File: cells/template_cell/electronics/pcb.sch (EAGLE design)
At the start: 28 parts, among them M1 M02PTH3, M2 M02PTH3, Q1 MOSFET-NCHANNEL2N7000, Q2 MOSFET-NCHANNEL2N7000, SW0 M01PTH_LONGPAD, SW1 M02PTH3, SW2 M02PTH3, SW3 M02PTH3, SW4 M02PTH3, SW5 M02PTH3

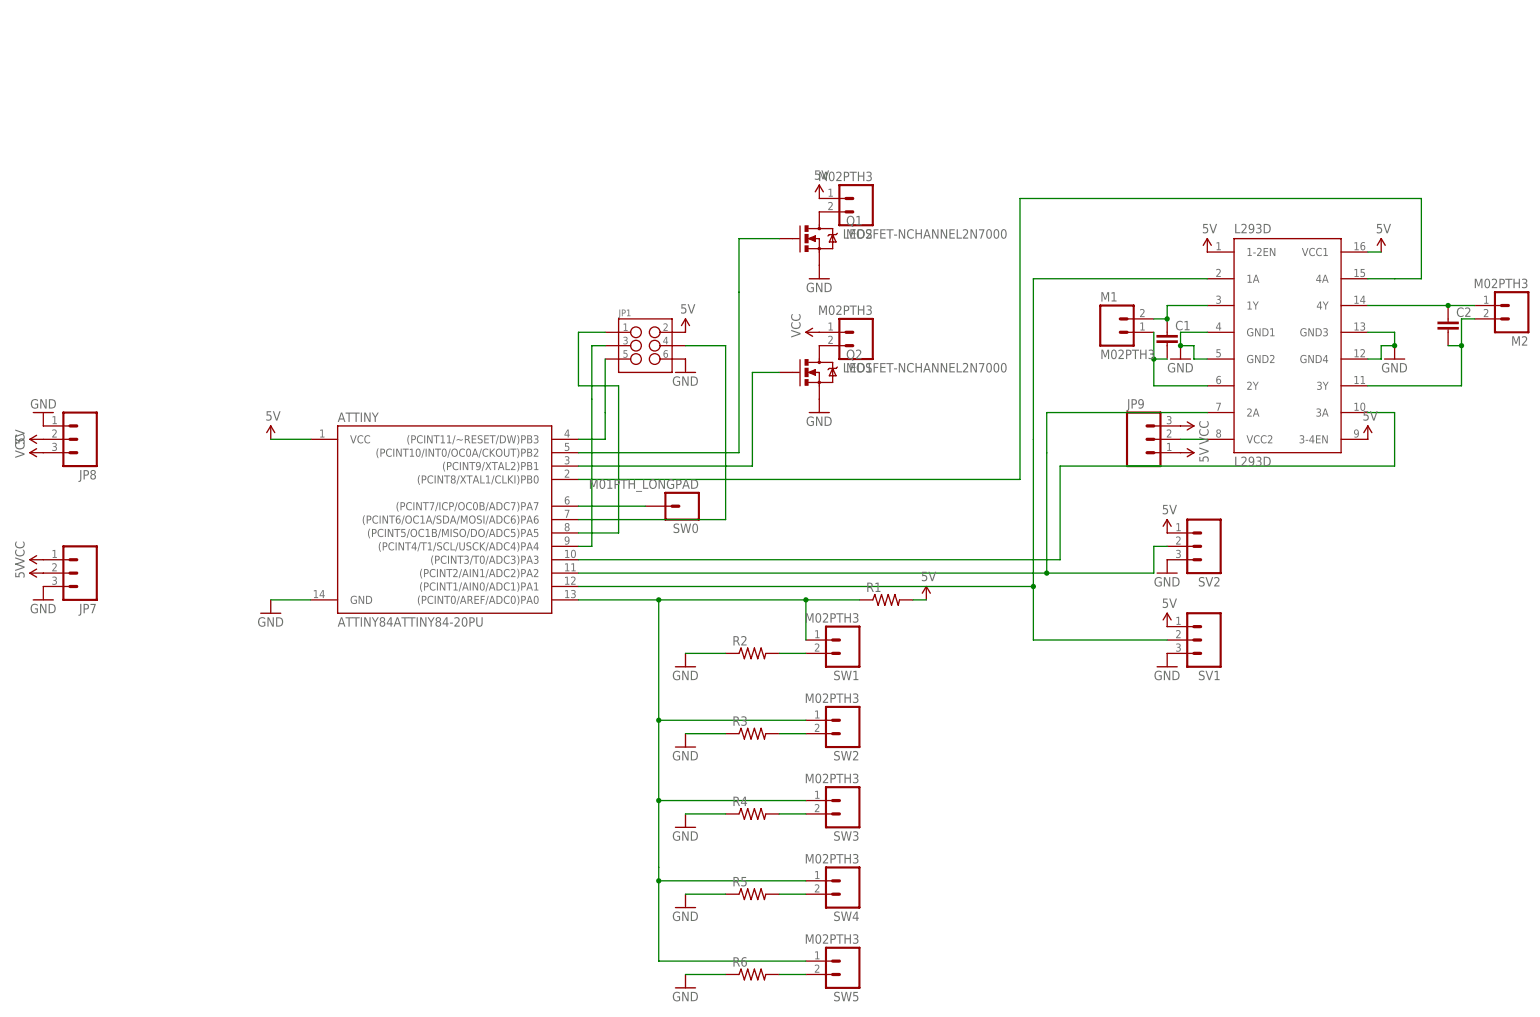
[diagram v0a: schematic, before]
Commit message: Moving electronics folder to template_cell
template_cell folder should contain all the things necessary to make a
cell, including the generic things like the electronics and basic
reusable parts.
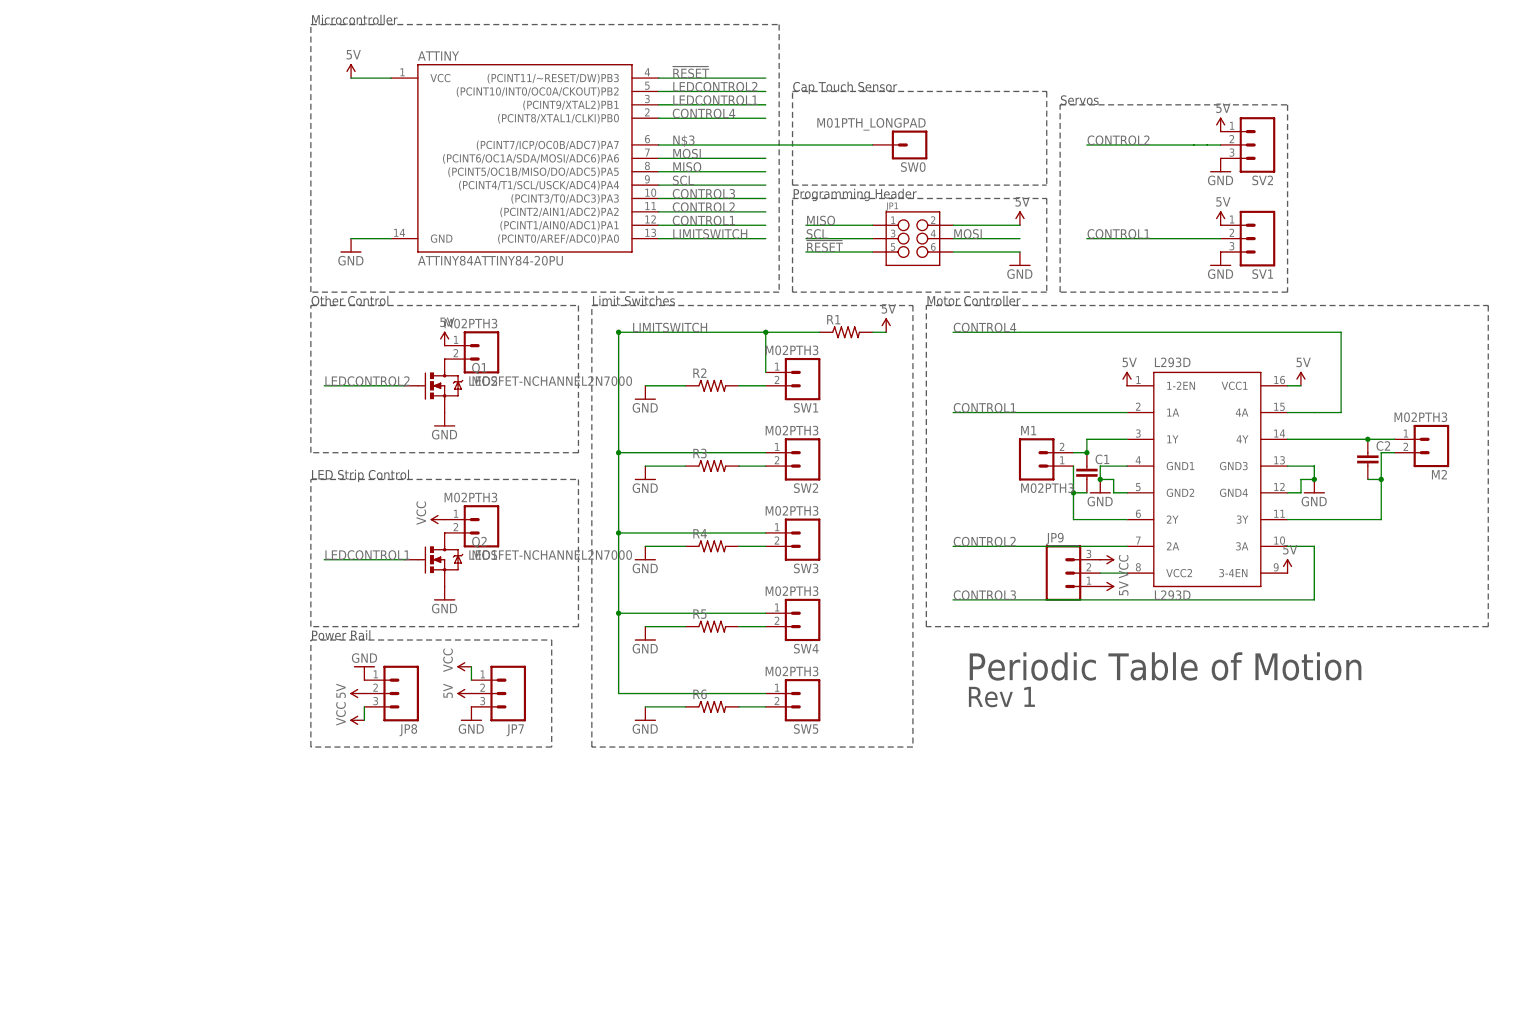
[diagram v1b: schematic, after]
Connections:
- net N$10 renamed LIMITSWITCH
- net N$11 renamed CONTROL1
- net N$14 renamed MOSI
- net N$15 renamed !RESET
- net N$16 renamed MISO
- net N$2 renamed CONTROL2
- net N$20 renamed LEDCONTROL1
- net N$21 renamed LEDCONTROL2
- net N$4 renamed CONTROL3
- net N$8 renamed SCL
- net N$9 renamed CONTROL4
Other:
- note added: "Cap Touch Sensor"
- note added: "LED Strip Control"
- note added: "Limit Switches"
- note added: "Microcontroller"
- note added: "Motor Controller"
- note added: "Other Control"
- note added: "Periodic Table of Motion"
- note added: "Power Rail"
- note added: "Programming Header"
- note added: "Rev 1"
- note added: "Servos"
- moved on the sheet: ATTINY, C1, C2, JP1, JP7, JP8, JP9, L293D, LED1, LED2, M1, M2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
